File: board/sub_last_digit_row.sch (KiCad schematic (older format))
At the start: 100 parts, among them Q801 Q_PMOS_GSD, Q802 Q_PMOS_GSD, Q803 Q_PMOS_GSD, Q804 Q_PMOS_GSD, Q805 Q_PMOS_GSD, Q806 Q_PMOS_GSD, Q807 Q_PMOS_GSD, U801 TPIC6D595, U802 TPIC6D595, U803 TPIC6D595

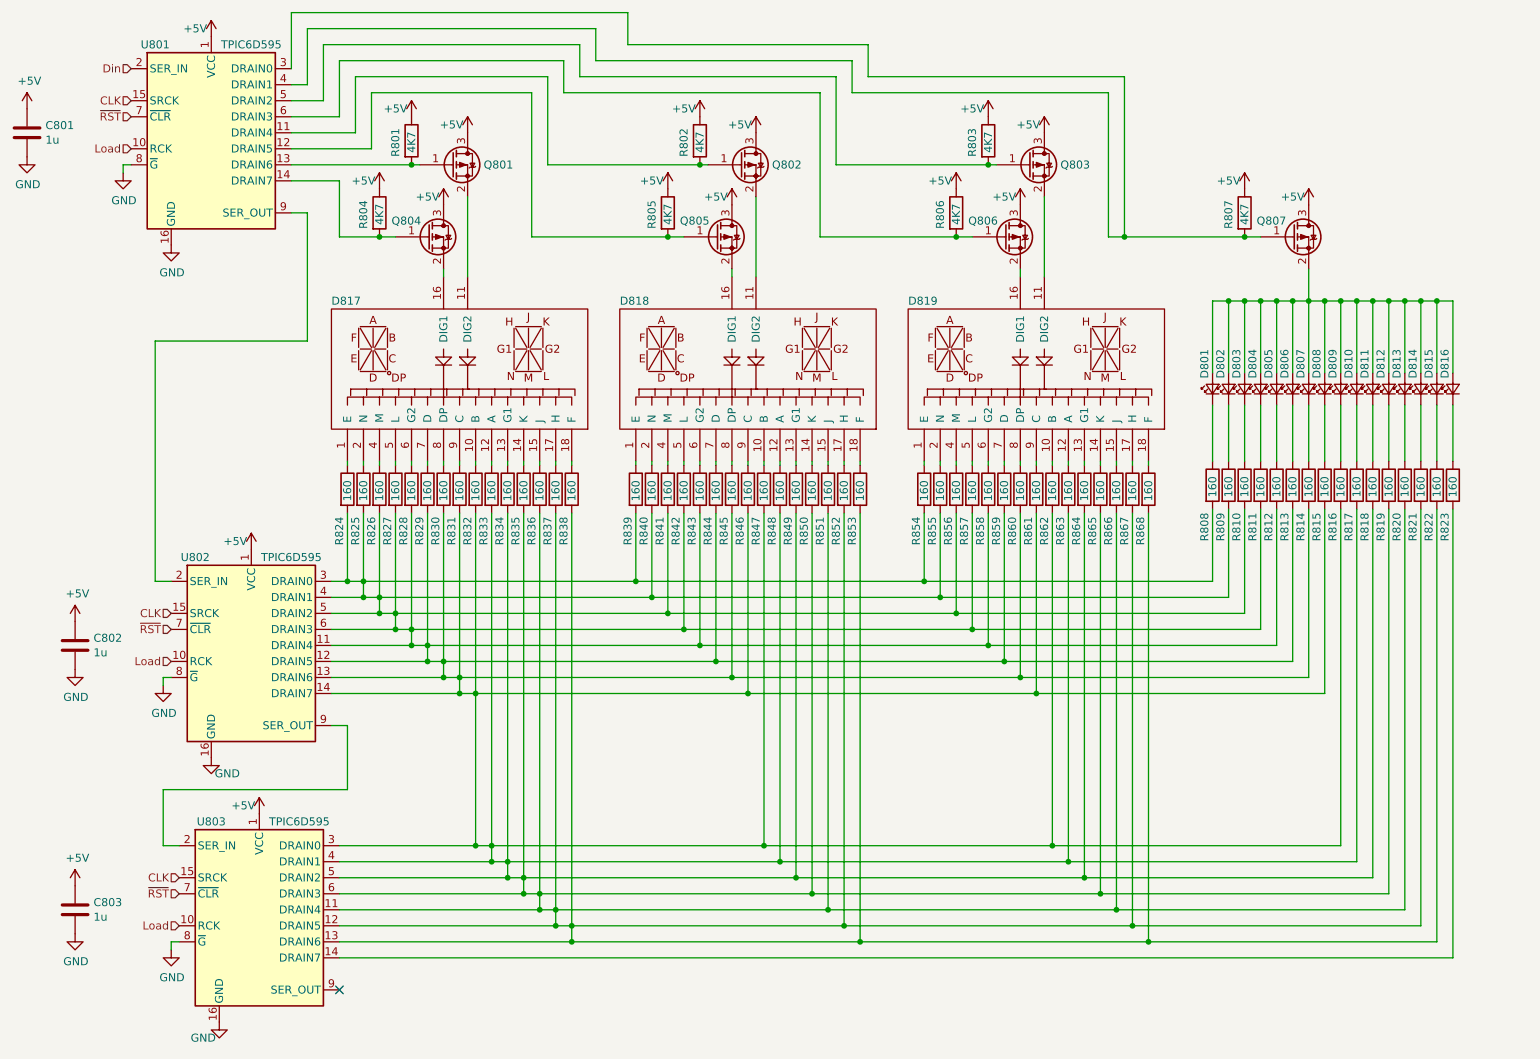
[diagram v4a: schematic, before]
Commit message: Started picking footprints. Merged many components.
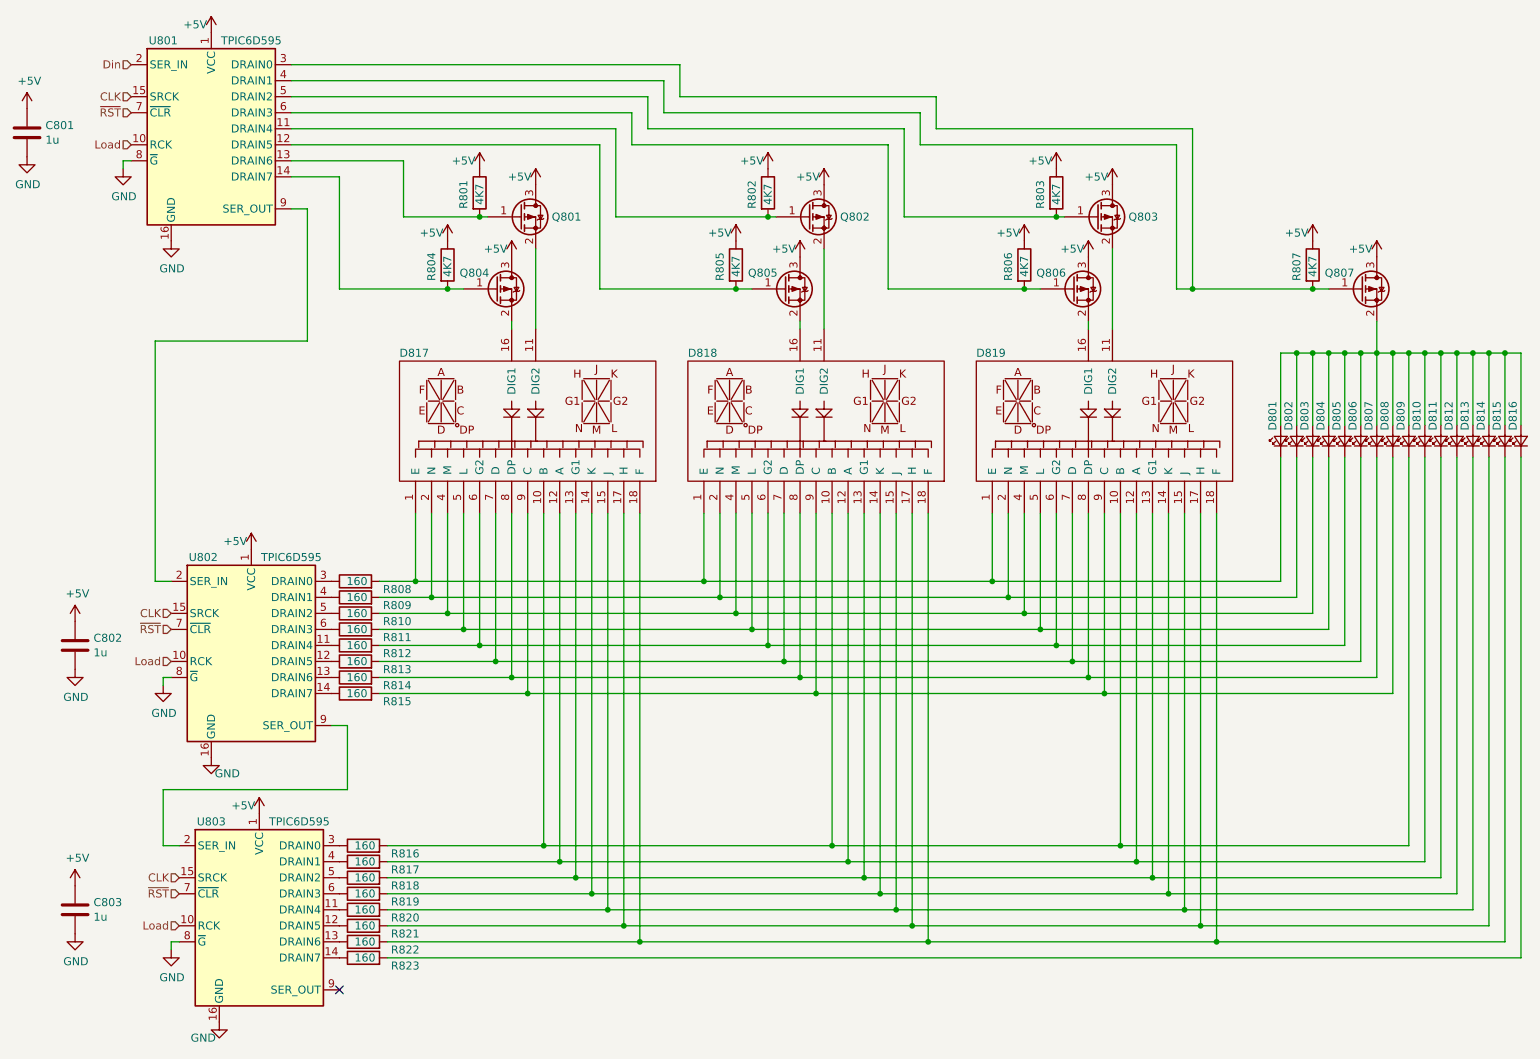
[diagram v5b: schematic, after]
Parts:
- removed R824, R825, R826, R827, R828, R829, R830, R831, R832, R833, R834, R835, R836, R837, R838, R839, R840, R841, R842, R843, R844, R845, R846, R847, R848, R849, R850, R851, R852, R853, R854, R855, R856, R857, R858, R859, R860, R861, R862, R863, R864, R865, R866, R867, R868: 160, symbol Device:R
- U801, U802, U803: footprint (none) -> Package_SO:SOIC-16_3.9x9.9mm_P1.27mm
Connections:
- net at D817.1 (E): now also D801.1 (K), D818.1 (E), D819.1 (E), R808.2
- net at D817.2 (N): now also D802.1 (K), D818.2 (N), D819.2 (N), R809.2
- net at D817.4 (M): now also D803.1 (K), D818.4 (M), D819.4 (M), R810.2
- net at D817.5 (L): now also D804.1 (K), D818.5 (L), D819.5 (L), R811.2
- net at D817.6 (G2): now also D805.1 (K), D818.6 (G2), D819.6 (G2), R812.2
- net at D817.7 (D): now also D806.1 (K), D818.7 (D), D819.7 (D), R813.2
- net at D817.8 (DP): now also D807.1 (K), D818.8 (DP), D819.8 (DP), R814.2
- net at D817.9 (C): now also D808.1 (K), D818.9 (C), D819.9 (C), R815.2
- net at D817.10 (B): now also D809.1 (K), D818.10 (B), D819.10 (B), R816.2
- net at D817.12 (A): now also D810.1 (K), D818.12 (A), D819.12 (A), R817.2
- net at D817.13 (G1): now also D811.1 (K), D818.13 (G1), D819.13 (G1), R818.2
- net at D817.14 (K): now also D812.1 (K), D818.14 (K), D819.14 (K), R819.2
- net at D817.15 (J): now also D813.1 (K), D818.15 (J), D819.15 (J), R820.2
- net at D817.17 (H): now also D814.1 (K), D818.17 (H), D819.17 (H), R821.2
- net at D817.18 (F): now also D815.1 (K), D818.18 (F), D819.18 (F), R822.2
- net at R808.1: now also U802.3 (DRAIN0); no longer D801.1 (K)
- net at R809.1: now also U802.4 (DRAIN1); no longer D802.1 (K)
- net at R810.1: now also U802.5 (DRAIN2); no longer D803.1 (K)
- net at R811.1: now also U802.6 (DRAIN3); no longer D804.1 (K)
- net at R812.1: now also U802.11 (DRAIN4); no longer D805.1 (K)
- net at R813.1: now also U802.12 (DRAIN5); no longer D806.1 (K)
- net at R814.1: now also U802.13 (DRAIN6); no longer D807.1 (K)
- net at R815.1: now also U802.14 (DRAIN7); no longer D808.1 (K)
- net at R816.1: now also U803.3 (DRAIN0); no longer D809.1 (K)
- net at R817.1: now also U803.4 (DRAIN1); no longer D810.1 (K)
- net at R818.1: now also U803.5 (DRAIN2); no longer D811.1 (K)
- net at R819.1: now also U803.6 (DRAIN3); no longer D812.1 (K)
- net at R820.1: now also U803.11 (DRAIN4); no longer D813.1 (K)
- net at R821.1: now also U803.12 (DRAIN5); no longer D814.1 (K)
- net at R822.1: now also U803.13 (DRAIN6); no longer D815.1 (K)
- net at D816.1 (K): now also R823.2; no longer R823.1
- net at U803.14 (DRAIN7): now also R823.1; no longer R823.2
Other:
- moved on the sheet: D801, D802, D803, D804, D805, D806, D807, D808, D809, D810, D811, D812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

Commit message: More footprints done. Went with simpler test-pads.
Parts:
- Q801, Q802, Q803, Q804, Q805, Q806, Q807: footprint (none) -> Package_TO_SOT_SMD:SOT-23
- R808, R809, R810, R811, R812, R813, R814, R815, R816, R817, R818, R819, R820, R821, R822, R823: footprint (none) -> Resistor_SMD:R_1206_3216Metric
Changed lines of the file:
@@
 $Descr A4 11693 8268
 encoding utf-8
-Sheet 8 15
+Sheet 8 14
 Title ""
 Date ""
@@
 F 0 "Q807" H 8800 2375 50  0000 L CNN
 F 1 "Q_PMOS_GSD" H 9231 2230 50  0001 L CNN
-F 2 "" H 9225 2375 50  0001 C CNN
+F 2 "Package_TO_SOT_SMD:SOT-23" H 9225 2375 50  0001 C CNN
 F 3 "~" H 9025 2275 50  0001 C CNN
 	1    9025 2275
@@
 F 0 "Q804" H 3400 2375 50  0000 L CNN
 F 1 "Q_PMOS_GSD" H 3831 2230 50  0001 L CNN
-F 2 "" H 3825 2375 50  0001 C CNN
+F 2 "Package_TO_SOT_SMD:SOT-23" H 3825 2375 50  0001 C CNN
 F 3 "~" H 3625 2275 50  0001 C CNN
 	1    3625 2275
@@
 F 0 "Q801" H 3975 1825 50  0000 L CNN
 F 1 "Q_PMOS_GSD" H 3981 1780 50  0001 L CNN
-F 2 "" H 3975 1925 50  0001 C CNN
+F 2 "Package_TO_SOT_SMD:SOT-23" H 3975 1925 50  0001 C CNN
 F 3 "~" H 3775 1825 50  0001 C CNN
 	1    3775 1825
@@
 F 0 "Q805" H 5200 2375 50  0000 L CNN
 F 1 "Q_PMOS_GSD" H 5631 2230 50  0001 L CNN
-F 2 "" H 5625 2375 50  0001 C CNN
+F 2 "Package_TO_SOT_SMD:SOT-23" H 5625 2375 50  0001 C CNN
 F 3 "~" H 5425 2275 50  0001 C CNN
 	1    5425 2275
@@
 F 0 "Q802" H 5775 1825 50  0000 L CNN
 F 1 "Q_PMOS_GSD" H 5781 1780 50  0001 L CNN
-F 2 "" H 5775 1925 50  0001 C CNN
+F 2 "Package_TO_SOT_SMD:SOT-23" H 5775 1925 50  0001 C CNN
 F 3 "~" H 5575 1825 50  0001 C CNN
 	1    5575 1825
@@
 F 0 "Q806" H 7000 2375 50  0000 L CNN
 F 1 "Q_PMOS_GSD" H 7431 2230 50  0001 L CNN
-F 2 "" H 7425 2375 50  0001 C CNN
+F 2 "Package_TO_SOT_SMD:SOT-23" H 7425 2375 50  0001 C CNN
 F 3 "~" H 7225 2275 50  0001 C CNN
 	1    7225 2275
@@
 F 0 "Q803" H 7575 1825 50  0000 L CNN
 F 1 "Q_PMOS_GSD" H 7581 1780 50  0001 L CNN
-F 2 "" H 7575 1925 50  0001 C CNN
+F 2 "Package_TO_SOT_SMD:SOT-23" H 7575 1925 50  0001 C CNN
 F 3 "~" H 7375 1825 50  0001 C CNN
 	1    7375 1825
@@
 F 0 "R822" V 2750 6000 50  0000 L CNN
 F 1 "160" V 2800 6275 50  0000 L CNN
-F 2 "" V 2730 6350 50  0001 C CNN
+F 2 "Resistor_SMD:R_1206_3216Metric" V 2730 6350 50  0001 C CNN
 F 3 "~" H 2800 6350 50  0001 C CNN
 	1    2800 6350
@@
 F 0 "R821" V 2750 5900 50  0000 L CNN
 F 1 "160" V 2800 6175 50  0000 L CNN
-F 2 "" V 2730 6250 50  0001 C CNN
+F 2 "Resistor_SMD:R_1206_3216Metric" V 2730 6250 50  0001 C CNN
 F 3 "~" H 2800 6250 50  0001 C CNN
 	1    2800 6250
@@
 F 0 "R820" V 2750 5800 50  0000 L CNN
 F 1 "160" V 2800 6075 50  0000 L CNN
-F 2 "" V 2730 6150 50  0001 C CNN
+F 2 "Resistor_SMD:R_1206_3216Metric" V 2730 6150 50  0001 C CNN
 F 3 "~" H 2800 6150 50  0001 C CNN
 	1    2800 6150
@@
 F 0 "R819" V 2750 5700 50  0000 L CNN
 F 1 "160" V 2800 5975 50  0000 L CNN
-F 2 "" V 2730 6050 50  0001 C CNN
+F 2 "Resistor_SMD:R_1206_3216Metric" V 2730 6050 50  0001 C CNN
 F 3 "~" H 2800 6050 50  0001 C CNN
 	1    2800 6050
@@
 F 0 "R818" V 2750 5600 50  0000 L CNN
 F 1 "160" V 2800 5875 50  0000 L CNN
-F 2 "" V 2730 5950 50  0001 C CNN
+F 2 "Resistor_SMD:R_1206_3216Metric" V 2730 5950 50  0001 C CNN
 F 3 "~" H 2800 5950 50  0001 C CNN
 	1    2800 5950
@@
 F 0 "R817" V 2750 5500 50  0000 L CNN
 F 1 "160" V 2800 5775 50  0000 L CNN
-F 2 "" V 2730 5850 50  0001 C CNN
+F 2 "Resistor_SMD:R_1206_3216Metric" V 2730 5850 50  0001 C CNN
 F 3 "~" H 2800 5850 50  0001 C CNN
 	1    2800 5850
@@
 F 0 "R816" V 2750 5400 50  0000 L CNN
 F 1 "160" V 2800 5675 50  0000 L CNN
-F 2 "" V 2730 5750 50  0001 C CNN
+F 2 "Resistor_SMD:R_1206_3216Metric" V 2730 5750 50  0001 C CNN
 F 3 "~" H 2800 5750 50  0001 C CNN
 	1    2800 5750
@@
 F 0 "R815" V 2700 4450 50  0000 L CNN
 F 1 "160" V 2750 4725 50  0000 L CNN
-F 2 "" V 2680 4800 50  0001 C CNN
+F 2 "Resistor_SMD:R_1206_3216Metric" V 2680 4800 50  0001 C CNN
 F 3 "~" H 2750 4800 50  0001 C CNN
 	1    2750 4800
@@
 F 0 "R814" V 2700 4350 50  0000 L CNN
 F 1 "160" V 2750 4625 50  0000 L CNN
-F 2 "" V 2680 4700 50  0001 C CNN
+F 2 "Resistor_SMD:R_1206_3216Metric" V 2680 4700 50  0001 C CNN
 F 3 "~" H 2750 4700 50  0001 C CNN
 	1    2750 4700
@@
 F 0 "R813" V 2700 4250 50  0000 L CNN
 F 1 "160" V 2750 4525 50  0000 L CNN
-F 2 "" V 2680 4600 50  0001 C CNN
+F 2 "Resistor_SMD:R_1206_3216Metric" V 2680 4600 50  0001 C CNN
 F 3 "~" H 2750 4600 50  0001 C CNN
 	1    2750 4600
@@
 F 0 "R812" V 2700 4150 50  0000 L CNN
 F 1 "160" V 2750 4425 50  0000 L CNN
-F 2 "" V 2680 4500 50  0001 C CNN
+F 2 "Resistor_SMD:R_1206_3216Metric" V 2680 4500 50  0001 C CNN
 F 3 "~" H 2750 4500 50  0001 C CNN
 	1    2750 4500
@@
 F 0 "R811" V 2700 4050 50  0000 L CNN
 F 1 "160" V 2750 4325 50  0000 L CNN
-F 2 "" V 2680 4400 50  0001 C CNN
+F 2 "Resistor_SMD:R_1206_3216Metric" V 2680 4400 50  0001 C CNN
 F 3 "~" H 2750 4400 50  0001 C CNN
 	1    2750 4400
@@
 F 0 "R810" V 2700 3950 50  0000 L CNN
 F 1 "160" V 2750 4225 50  0000 L CNN
-F 2 "" V 2680 4300 50  0001 C CNN
+F 2 "Resistor_SMD:R_1206_3216Metric" V 2680 4300 50  0001 C CNN
 F 3 "~" H 2750 4300 50  0001 C CNN
 	1    2750 4300
@@
 F 0 "R809" V 2700 3850 50  0000 L CNN
 F 1 "160" V 2750 4125 50  0000 L CNN
-F 2 "" V 2680 4200 50  0001 C CNN
+F 2 "Resistor_SMD:R_1206_3216Metric" V 2680 4200 50  0001 C CNN
 F 3 "~" H 2750 4200 50  0001 C CNN
 	1    2750 4200
@@
 F 0 "R808" V 2700 3750 50  0000 L CNN
 F 1 "160" V 2750 4025 50  0000 L CNN
-F 2 "" V 2680 4100 50  0001 C CNN
+F 2 "Resistor_SMD:R_1206_3216Metric" V 2680 4100 50  0001 C CNN
 F 3 "~" H 2750 4100 50  0001 C CNN
 	1    2750 4100
@@
 F 0 "R823" V 2750 6100 50  0000 L CNN
 F 1 "160" V 2800 6375 50  0000 L CNN
-F 2 "" V 2730 6450 50  0001 C CNN
+F 2 "Resistor_SMD:R_1206_3216Metric" V 2730 6450 50  0001 C CNN
 F 3 "~" H 2800 6450 50  0001 C CNN
 	1    2800 6450

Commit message: Most footprints associated
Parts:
- C801, C802, C803: footprint (none) -> Capacitor_SMD:C_0603_1608Metric
- D801, D802, D803, D804, D805, D806, D807, D808, D809, D810, D811, D812, D813, D814, D815, D816: footprint (none) -> LED_SMD:LED_0805_2012Metric
- R801, R802, R803, R804, R805, R806, R807: footprint (none) -> Resistor_SMD:R_0603_1608Metric
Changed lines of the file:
@@
 F 0 "R807" V 8625 2025 50  0000 L CNN
 F 1 "4K7" V 8725 2050 50  0000 L CNN
-F 2 "" V 8655 2125 50  0001 C CNN
+F 2 "Resistor_SMD:R_0603_1608Metric" V 8655 2125 50  0001 C CNN
 F 3 "~" H 8725 2125 50  0001 C CNN
 	1    8725 2125
@@
 F 0 "D801" H 8775 3275 50  0000 R CNN
 F 1 "LED_Small" V 8480 3157 50  0001 R CNN
-F 2 "" V 8525 3225 50  0001 C CNN
+F 2 "LED_SMD:LED_0805_2012Metric" V 8525 3225 50  0001 C CNN
 F 3 "~" V 8525 3225 50  0001 C CNN
 	1    8525 3225
@@
 F 0 "D802" H 8875 3275 50  0000 R CNN
 F 1 "LED_Small" V 8580 3157 50  0001 R CNN
-F 2 "" V 8625 3225 50  0001 C CNN
+F 2 "LED_SMD:LED_0805_2012Metric" V 8625 3225 50  0001 C CNN
 F 3 "~" V 8625 3225 50  0001 C CNN
 	1    8625 3225
@@
 F 0 "D815" H 10175 3275 50  0000 R CNN
 F 1 "LED_Small" V 9880 3157 50  0001 R CNN
-F 2 "" V 9925 3225 50  0001 C CNN
+F 2 "LED_SMD:LED_0805_2012Metric" V 9925 3225 50  0001 C CNN
 F 3 "~" V 9925 3225 50  0001 C CNN
 	1    9925 3225
@@
 F 0 "D814" H 10075 3275 50  0000 R CNN
 F 1 "LED_Small" V 9780 3157 50  0001 R CNN
-F 2 "" V 9825 3225 50  0001 C CNN
+F 2 "LED_SMD:LED_0805_2012Metric" V 9825 3225 50  0001 C CNN
 F 3 "~" V 9825 3225 50  0001 C CNN
 	1    9825 3225
@@
 F 0 "D813" H 9975 3275 50  0000 R CNN
 F 1 "LED_Small" V 9680 3157 50  0001 R CNN
-F 2 "" V 9725 3225 50  0001 C CNN
+F 2 "LED_SMD:LED_0805_2012Metric" V 9725 3225 50  0001 C CNN
 F 3 "~" V 9725 3225 50  0001 C CNN
 	1    9725 3225
@@
 F 0 "D812" H 9875 3275 50  0000 R CNN
 F 1 "LED_Small" V 9580 3157 50  0001 R CNN
-F 2 "" V 9625 3225 50  0001 C CNN
+F 2 "LED_SMD:LED_0805_2012Metric" V 9625 3225 50  0001 C CNN
 F 3 "~" V 9625 3225 50  0001 C CNN
 	1    9625 3225
@@
 F 0 "D811" H 9775 3275 50  0000 R CNN
 F 1 "LED_Small" V 9480 3157 50  0001 R CNN
-F 2 "" V 9525 3225 50  0001 C CNN
+F 2 "LED_SMD:LED_0805_2012Metric" V 9525 3225 50  0001 C CNN
 F 3 "~" V 9525 3225 50  0001 C CNN
 	1    9525 3225
@@
 F 0 "D810" H 9675 3275 50  0000 R CNN
 F 1 "LED_Small" V 9380 3157 50  0001 R CNN
-F 2 "" V 9425 3225 50  0001 C CNN
+F 2 "LED_SMD:LED_0805_2012Metric" V 9425 3225 50  0001 C CNN
 F 3 "~" V 9425 3225 50  0001 C CNN
 	1    9425 3225
@@
 F 0 "D809" H 9575 3275 50  0000 R CNN
 F 1 "LED_Small" V 9280 3157 50  0001 R CNN
-F 2 "" V 9325 3225 50  0001 C CNN
+F 2 "LED_SMD:LED_0805_2012Metric" V 9325 3225 50  0001 C CNN
 F 3 "~" V 9325 3225 50  0001 C CNN
 	1    9325 3225
@@
 F 0 "D808" H 9475 3275 50  0000 R CNN
 F 1 "LED_Small" V 9180 3157 50  0001 R CNN
-F 2 "" V 9225 3225 50  0001 C CNN
+F 2 "LED_SMD:LED_0805_2012Metric" V 9225 3225 50  0001 C CNN
 F 3 "~" V 9225 3225 50  0001 C CNN
 	1    9225 3225
@@
 F 0 "D807" H 9375 3275 50  0000 R CNN
 F 1 "LED_Small" V 9080 3157 50  0001 R CNN
-F 2 "" V 9125 3225 50  0001 C CNN
+F 2 "LED_SMD:LED_0805_2012Metric" V 9125 3225 50  0001 C CNN
 F 3 "~" V 9125 3225 50  0001 C CNN
 	1    9125 3225
@@
 F 0 "D806" H 9275 3275 50  0000 R CNN
 F 1 "LED_Small" V 8980 3157 50  0001 R CNN
-F 2 "" V 9025 3225 50  0001 C CNN
+F 2 "LED_SMD:LED_0805_2012Metric" V 9025 3225 50  0001 C CNN
 F 3 "~" V 9025 3225 50  0001 C CNN
 	1    9025 3225
@@
 F 0 "D805" H 9175 3275 50  0000 R CNN
 F 1 "LED_Small" V 8880 3157 50  0001 R CNN
-F 2 "" V 8925 3225 50  0001 C CNN
+F 2 "LED_SMD:LED_0805_2012Metric" V 8925 3225 50  0001 C CNN
 F 3 "~" V 8925 3225 50  0001 C CNN
 	1    8925 3225
@@
 F 0 "D804" H 9075 3275 50  0000 R CNN
 F 1 "LED_Small" V 8780 3157 50  0001 R CNN
-F 2 "" V 8825 3225 50  0001 C CNN
+F 2 "LED_SMD:LED_0805_2012Metric" V 8825 3225 50  0001 C CNN
 F 3 "~" V 8825 3225 50  0001 C CNN
 	1    8825 3225
@@
 F 0 "D803" H 8975 3275 50  0000 R CNN
 F 1 "LED_Small" V 8680 3157 50  0001 R CNN
-F 2 "" V 8725 3225 50  0001 C CNN
+F 2 "LED_SMD:LED_0805_2012Metric" V 8725 3225 50  0001 C CNN
 F 3 "~" V 8725 3225 50  0001 C CNN
 	1    8725 3225
@@
 F 0 "D816" H 10275 3275 50  0000 R CNN
 F 1 "LED_Small" V 9980 3157 50  0001 R CNN
-F 2 "" V 10025 3225 50  0001 C CNN
+F 2 "LED_SMD:LED_0805_2012Metric" V 10025 3225 50  0001 C CNN
 F 3 "~" V 10025 3225 50  0001 C CNN
 	1    10025 3225
@@
 F 0 "R804" V 3225 2025 50  0000 L CNN
 F 1 "4K7" V 3325 2050 50  0000 L CNN
-F 2 "" V 3255 2125 50  0001 C CNN
+F 2 "Resistor_SMD:R_0603_1608Metric" V 3255 2125 50  0001 C CNN
 F 3 "~" H 3325 2125 50  0001 C CNN
 	1    3325 2125
@@
 F 0 "R801" V 3425 1575 50  0000 L CNN
 F 1 "4K7" V 3525 1600 50  0000 L CNN
-F 2 "" V 3455 1675 50  0001 C CNN
+F 2 "Resistor_SMD:R_0603_1608Metric" V 3455 1675 50  0001 C CNN
 F 3 "~" H 3525 1675 50  0001 C CNN
 	1    3525 1675
@@
 F 0 "R805" V 5025 2025 50  0000 L CNN
 F 1 "4K7" V 5125 2050 50  0000 L CNN
-F 2 "" V 5055 2125 50  0001 C CNN
+F 2 "Resistor_SMD:R_0603_1608Metric" V 5055 2125 50  0001 C CNN
 F 3 "~" H 5125 2125 50  0001 C CNN
 	1    5125 2125
@@
 F 0 "R802" V 5225 1575 50  0000 L CNN
 F 1 "4K7" V 5325 1600 50  0000 L CNN
-F 2 "" V 5255 1675 50  0001 C CNN
+F 2 "Resistor_SMD:R_0603_1608Metric" V 5255 1675 50  0001 C CNN
 F 3 "~" H 5325 1675 50  0001 C CNN
 	1    5325 1675
@@
 F 0 "R806" V 6825 2025 50  0000 L CNN
 F 1 "4K7" V 6925 2050 50  0000 L CNN
-F 2 "" V 6855 2125 50  0001 C CNN
+F 2 "Resistor_SMD:R_0603_1608Metric" V 6855 2125 50  0001 C CNN
 F 3 "~" H 6925 2125 50  0001 C CNN
 	1    6925 2125
@@
 F 0 "R803" V 7025 1575 50  0000 L CNN
 F 1 "4K7" V 7125 1600 50  0000 L CNN
-F 2 "" V 7055 1675 50  0001 C CNN
+F 2 "Resistor_SMD:R_0603_1608Metric" V 7055 1675 50  0001 C CNN
 F 3 "~" H 7125 1675 50  0001 C CNN
 	1    7125 1675
@@
 F 0 "C803" H 1115 6196 50  0000 L CNN
 F 1 "1u" H 1115 6105 50  0000 L CNN
-F 2 "" H 1038 6000 50  0001 C CNN
+F 2 "Capacitor_SMD:C_0603_1608Metric" H 1038 6000 50  0001 C CNN
 F 3 "~" H 1000 6150 50  0001 C CNN
 	1    1000 6150
@@
 F 0 "C802" H 1115 4546 50  0000 L CNN
 F 1 "1u" H 1115 4455 50  0000 L CNN
-F 2 "" H 1038 4350 50  0001 C CNN
+F 2 "Capacitor_SMD:C_0603_1608Metric" H 1038 4350 50  0001 C CNN
 F 3 "~" H 1000 4500 50  0001 C CNN
 	1    1000 4500
@@
 F 0 "C801" H 815 1346 50  0000 L CNN
 F 1 "1u" H 815 1255 50  0000 L CNN
-F 2 "" H 738 1150 50  0001 C CNN
+F 2 "Capacitor_SMD:C_0603_1608Metric" H 738 1150 50  0001 C CNN
 F 3 "~" H 700 1300 50  0001 C CNN
 	1    700  1300
